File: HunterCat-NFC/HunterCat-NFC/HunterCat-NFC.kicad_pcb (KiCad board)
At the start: 2 copper layers, 112 x 33.5 mm, 74 parts, among them J1 Battery, J2 Conn_01x06_Female, P1 USB_C_Plug_USB2.0, Q1 DMG3415U-7, SW1 RESET, SW2 GPIO, SW3 GPIO1, SW4 GPIO2, U1 ATSAMD21E18A, U2 PN7150B0HN_C11002E-PN7150B0HN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

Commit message: new size
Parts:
- removed the REF** at (107.7, 106.1)
- removed the REF** at (107.7, 78.4)
- L3: moved to B.Cu
- moved G*** 77.8 mm to (91.4, 92.3), turned to 90 degrees
- moved svg2mod 48.0 mm to (101.9, 94.2)
- moved L3 32.8 mm to (137.1, 92.0), turned to 180 degrees
- moved REF** 32.4 mm to (155.8, 78.1)
- moved REF** 32.1 mm to (156.2, 106.5)
- moved REF** 18.5 mm to (151.3, 92.9)
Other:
- board size 112 x 33.5 mm -> 80.7 x 33.5 mm

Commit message: Change ant
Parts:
- removed C6: 1uF, Capacitor_SMD:C_0603_1608Metric_Pad1.05x0.95mm_HandSolder
- moved R21 8.76 mm to (128.4, 98.4)
- moved U5 7.78 mm to (125.5, 96.0)
- moved C24 6.38 mm to (104.9, 77.9)
- moved U4 6.17 mm to (107.7, 77.9)
- moved R20 4.49 mm to (115.5, 103.4), turned to 0 degrees
- moved C25 4.11 mm to (121.3, 105.8), turned to 270 degrees
- moved U1 3.44 mm to (118.8, 95.2)
- moved P1 3.44 mm to (117.8, 82.0)
- moved Q1 2.58 mm to (110.9, 83.5), turned to 90 degrees
- moved R16 2.49 mm to (110.7, 77.7), turned to 90 degrees
- moved C9 2.11 mm to (131.1, 100.1)
- moved R9 2.02 mm to (119.8, 88.7)
- moved F1 1.95 mm to (118.4, 88.7)
- moved C1 1.70 mm to (118.2, 102.2)
- moved U2 1.54 mm to (133.9, 93.1)
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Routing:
- net GND: track 162.3 -> 107.2 mm, vias 12 -> 13
- net /GPIO2: track 38.9 -> 61.6 mm
- net /MISO: track 27.5 -> 5.25 mm
- net /SCK: track 15.2 -> 5.07 mm
- net /MOSI: track 14.2 -> 4.42 mm
- net /SCL: track 17.0 -> 25.5 mm
- net /CLK: track 18.7 -> 26.8 mm
- net /IRQ: track 16.4 -> 24.4 mm
- net /RST: track 49.9 -> 56.8 mm
- net /VEN: track 41.3 -> 35.0 mm, vias 0 -> 4
- net +BATT: track 77.2 -> 82.8 mm, vias 6 -> 5
- net /LED2: track 11.7 -> 6.52 mm
- net /LED3: track 12.3 -> 7.80 mm
- net Net-(L3-Pad2): track 2.59 -> 6.56 mm, vias 0 -> 1
- net /LED1: track 10.3 -> 6.69 mm
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
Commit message: last revision
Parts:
- moved D1 1.57 mm to (110.0, 97.0)
- moved D3 1.57 mm to (110.0, 99.0)
- moved D4 1.57 mm to (110.0, 101.1)
- moved R20 0.82 mm to (114.7, 103.6)
- moved R19 0.82 mm to (114.7, 102.1)
- moved C8 0.80 mm to (134.5, 101.3)
- moved C9 0.53 mm to (131.0, 99.6)
- moved U1 0.22 mm to (118.6, 95.2)
- moved C1 0.12 mm to (118.3, 102.3)
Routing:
- net +BATT: track 82.8 -> 50.9 mm
- net GND: track 107.2 -> 121.1 mm, vias 13 -> 16
- net /LED2: track 6.52 -> 9.02 mm
- net /LED3: track 7.80 -> 9.92 mm
- net /LED1: track 6.69 -> 8.68 mm
- net Net-(C8-Pad1): track 16.4 -> 14.6 mm
- net /SDA: track 21.6 -> 23.4 mm
- net /RXP: track 20.3 -> 22.0 mm
- net /RST: track 56.8 -> 55.1 mm
- net Net-(D4-Pad1): track 3.89 -> 2.34 mm
- net Net-(D3-Pad1): track 4.18 -> 2.84 mm
- net +3V3: track 108.6 -> 109.9 mm
- net /SWDIO: track 17.6 -> 18.8 mm
- net Net-(D1-Pad1): track 3.37 -> 2.25 mm
- net /VEN: track 35.0 -> 36.0 mm
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
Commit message: Last Revision
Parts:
- moved C10 1.04 mm to (144.5, 85.4)
- moved C9 0.18 mm to (131.0, 99.4)
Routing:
- net +BATT: track 50.9 -> 69.9 mm, vias 5 -> 7
- net /RST: track 55.1 -> 60.0 mm
- net +3V3: track 109.9 -> 107.3 mm
- net GND: track 121.1 -> 123.6 mm
- net Net-(C10-Pad1): track 3.13 -> 4.20 mm
- net /RXP: track 22.0 -> 23.0 mm

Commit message: Change Position
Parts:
- moved C4 31.3 mm to (158.3, 63.9)
- moved R3 31.3 mm to (152.8, 61.4)
- moved C3 31.3 mm to (153.0, 63.9)
- moved R5 31.3 mm to (153.2, 66.4)
- moved Y1 31.1 mm to (155.6, 64.2)
- moved C24 14.5 mm to (104.9, 92.4)
- moved R16 14.5 mm to (110.6, 92.2)
- moved U4 14.5 mm to (107.6, 92.3)
- moved R9 13.2 mm to (109.5, 80.5), turned to 0 degrees
- moved C23 10.5 mm to (109.6, 95.0), turned to 0 degrees
- moved R10 8.00 mm to (106.0, 86.2)
- moved U3 8.00 mm to (106.0, 83.5)
- moved D2 8.00 mm to (110.5, 83.3)
- moved R12 8.00 mm to (108.5, 83.5)
- moved C16 8.00 mm to (105.9, 80.6)
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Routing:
- net GND: track 123.6 -> 3.16 mm, vias 16 -> 2
- net +3V3: track 107.3 -> 0.00 mm, vias 10 -> 0
- net +BATT: track 69.9 -> 0.00 mm, vias 7 -> 0
- net /GPIO2: track 62.0 -> 0.00 mm, vias 2 -> 0
- net /RST: track 60.0 -> 0.00 mm, vias 3 -> 0
- net /GPIO1: track 39.1 -> 0.00 mm
- net /VEN: track 36.2 -> 0.00 mm, vias 4 -> 0
- net /CLK: track 26.9 -> 0.00 mm, vias 2 -> 0
- net VBUS: track 26.9 -> 0.00 mm
- net /SCL: track 25.8 -> 0.00 mm, vias 2 -> 0
- net /GPIO: track 25.7 -> 0.00 mm
- net /SWCLK: track 24.7 -> 0.00 mm, vias 2 -> 0
- net /IRQ: track 24.5 -> 0.00 mm, vias 2 -> 0
- net /SDA: track 23.4 -> 0.00 mm, vias 2 -> 0
- net /RXP: track 23.0 -> 0.00 mm, vias 2 -> 0
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- added copper zone on In1.Cu, net GND
- removed copper zone on F.Cu, net GND
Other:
- copper layers 2 -> 4

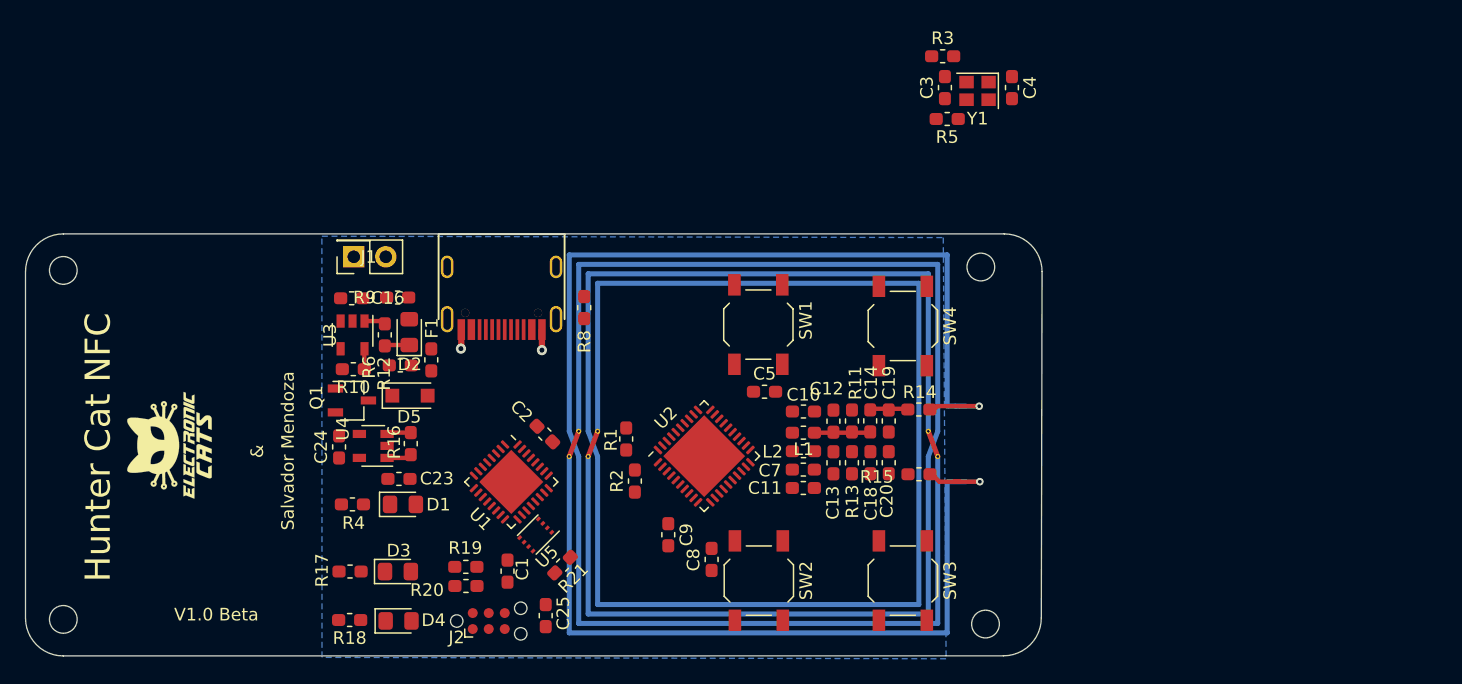
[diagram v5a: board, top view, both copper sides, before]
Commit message: update to 1.0v
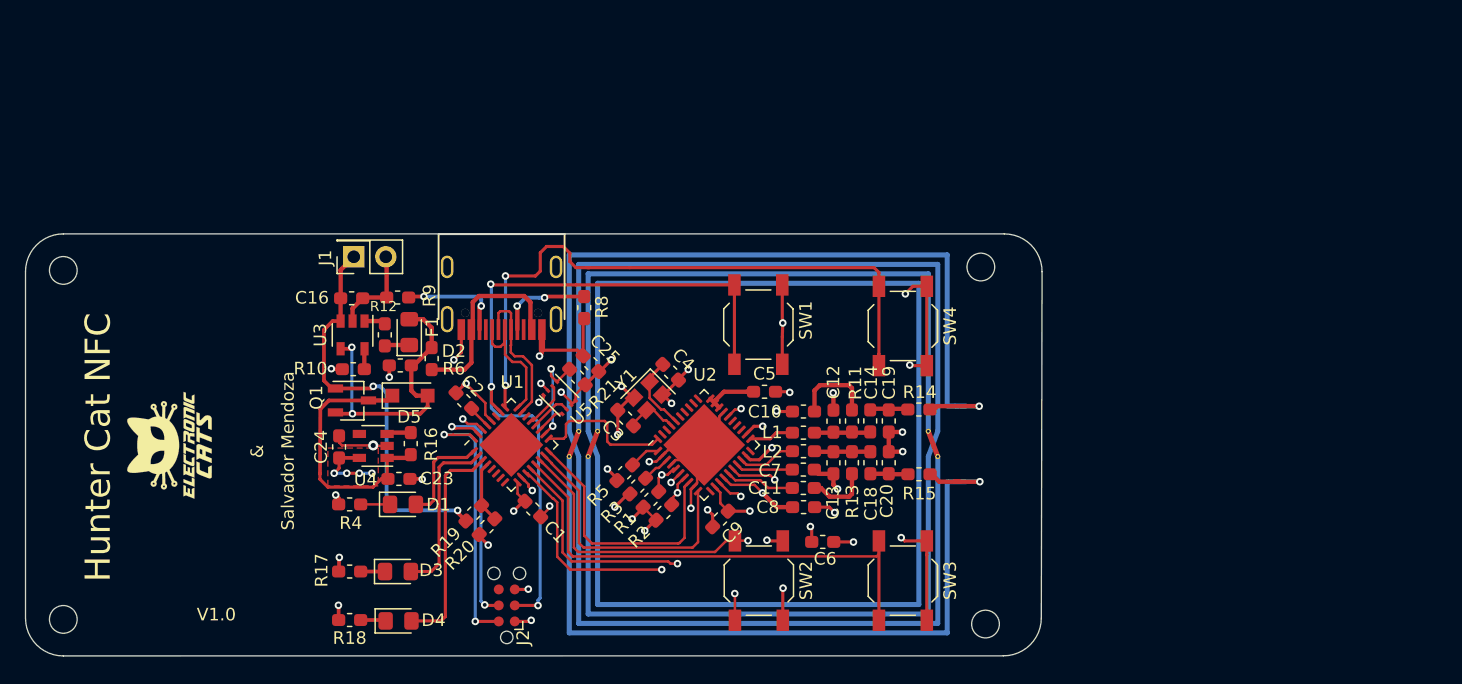
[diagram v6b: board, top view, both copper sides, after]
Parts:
- added C6: 1uF, Capacitor_SMD:C_0603_1608Metric_Pad1.05x0.95mm_HandSolder, F.Cu at (143.3, 100.0)
- moved R3 41.8 mm to (128.6, 95.5), turned to 225 degrees
- moved R5 38.0 mm to (127.6, 94.5), turned to 225 degrees
- moved C3 36.5 mm to (127.6, 90.1), turned to 135 degrees
- moved Y1 35.7 mm to (129.4, 88.4), turned to 225 degrees
- moved C4 35.3 mm to (131.2, 86.5), turned to 315 degrees
- moved C25 20.3 mm to (124.9, 85.8), turned to 135 degrees
- moved R21 15.0 mm to (123.8, 86.9), turned to 135 degrees
- moved REF** 13.4 mm to (138.0, 92.2)
- moved U5 12.0 mm to (122.2, 87.2), turned to 315 degrees
- moved C8 8.40 mm to (141.8, 97.2), turned to 0 degrees
- moved C2 6.95 mm to (114.8, 88.7), turned to 135 degrees
- moved C1 5.32 mm to (120.3, 97.3), turned to 315 degrees
- moved R1 5.17 mm to (129.6, 96.6), turned to 45 degrees
- moved R20 5.00 mm to (116.6, 98.7), turned to 225 degrees
- moved C9 4.32 mm to (135.2, 98.1), turned to 225 degrees
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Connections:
- SW2 pad 2: /GPIO -> /GPIO1
- SW3 pad 2: /GPIO1 -> /GPIO2
- SW4 pad 2: /GPIO2 -> /GPIO
- U1 pad 13: /IRQ -> /GPIO2
- U1 pad 14: /CLK -> /GPIO1
- U1 pad 15: /GPIO2 -> /VEN
- U1 pad 16: /GPIO1 -> /IRQ
- U1 pad 17: /GPIO -> /CLK
- U1 pad 25: Net-(U1-Pad25) -> /GPIO
- U1 pad 5: /VEN -> Net-(U1-Pad5)
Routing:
- net GND: track 3.16 -> 117.2 mm, vias 2 -> 38
- net /RST: track 0.00 -> 58.6 mm, vias 0 -> 3
- net /GPIO: track 0.00 -> 50.7 mm, vias 0 -> 2
- net +BATT: track 0.00 -> 46.3 mm, vias 0 -> 4
- net /GPIO2: track 0.00 -> 40.2 mm
- net /GPIO1: track 0.00 -> 29.7 mm, vias 0 -> 2
- net +3V3: track 0.00 -> 27.9 mm, vias 0 -> 15
- net /SDA: track 0.00 -> 26.7 mm, vias 0 -> 2
- net /SCL: track 0.00 -> 25.4 mm, vias 0 -> 2
- net VBUS: track 0.00 -> 24.0 mm, vias 0 -> 2
- net /VEN: track 0.00 -> 21.9 mm
- net /SWDIO: track 0.00 -> 21.4 mm, vias 0 -> 2
- net /IRQ: track 0.00 -> 20.8 mm
- net /SWCLK: track 0.00 -> 19.8 mm, vias 0 -> 2
- net Net-(C23-Pad1): track 1.62 -> 21.0 mm
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- added copper zone on F.Cu, net +3V3
- added copper zone on In2.Cu, net +3V3
- added copper zone on In2.Cu, net +BATT
- removed copper zone on B.Cu, net GND
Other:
- net class Default: clearance 0.25 -> 0.15
- net class sa removed
- net class source removed
- rule trace_clearance: 0.25 -> 0.15
- board text added: "V1.0"
- board text removed: "V1.0 Beta"

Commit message: new labels
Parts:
- removed the G*** at (115.9, 94.2)
- removed the REF** at (138.0, 92.2)
- removed svg2mod: electronic, Aesthetics:titule_electronic_med
- added REF**: OSHW-Logo_5.7x6mm_SilkScreen, Symbol:OSHW-Logo_5.7x6mm_SilkScreen, B.Cu at (114.9, 92.5)
- G***: moved to B.Cu
- turned G*** to 270 degrees
- renumbered SW4 to GPIO, SW2 to GPIO1, SW3 to GPIO2, SW1 to RST
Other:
- board text added: "If you have arrived here, you no longer have guarantee…"
- board text added: "now you have the power"

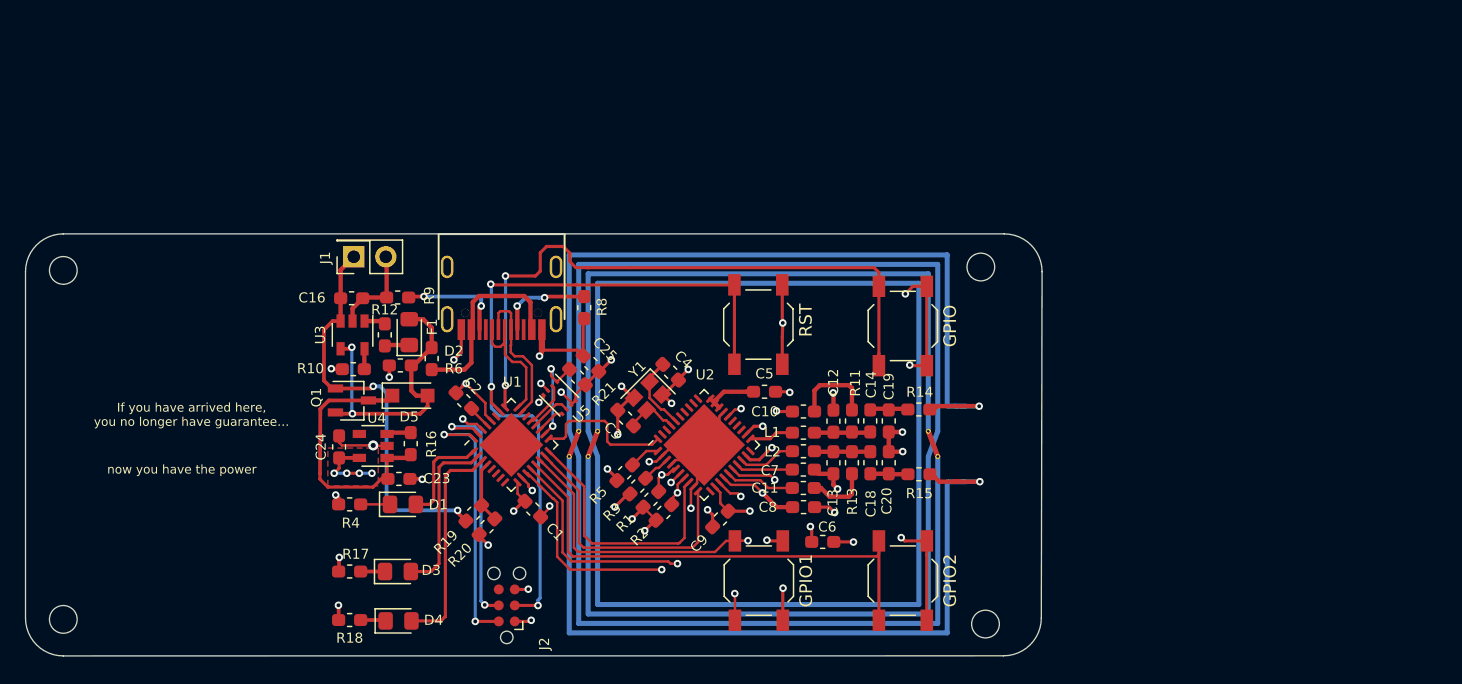
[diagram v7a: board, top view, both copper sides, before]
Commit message: Mounting Hole
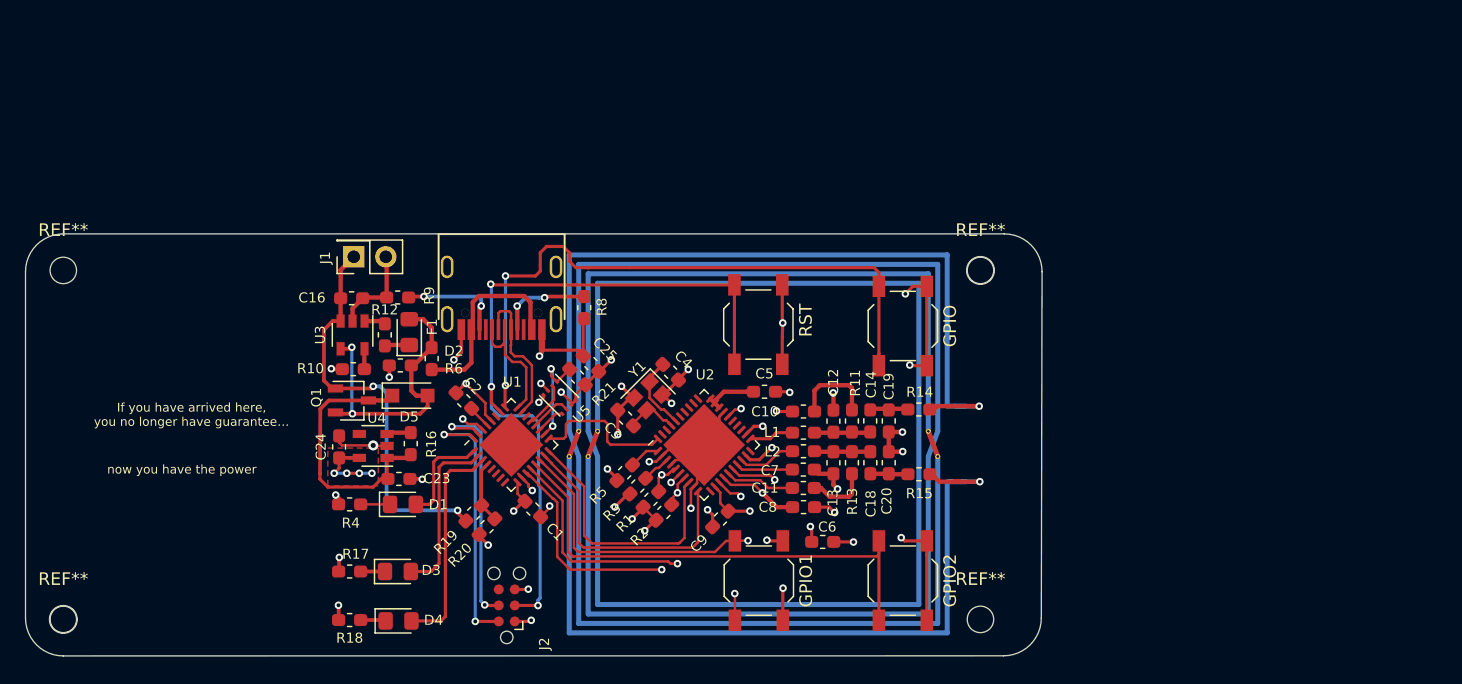
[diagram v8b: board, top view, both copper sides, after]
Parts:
- removed the REF** at (83.0, 78.4)
- removed the REF** at (156.2, 106.5)
- added REF**: MountingHole_2.1mm, MountingHole:MountingHole_2.1mm, F.Cu at (83.0, 106.1)
- added REF**: MountingHole_2.1mm, MountingHole:MountingHole_2.1mm, F.Cu at (83.0, 78.4)
- added REF**: MountingHole_2.1mm, MountingHole:MountingHole_2.1mm, F.Cu at (155.8, 106.1)
- added REF**: MountingHole_2.1mm, MountingHole:MountingHole_2.1mm, F.Cu at (155.8, 78.4)
- moved REF** 0.27 mm to (155.8, 78.4)
